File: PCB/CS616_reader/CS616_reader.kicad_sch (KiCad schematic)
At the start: 15 parts, among them J1 Conn_01x04_Socket, J2 Conn_01x04_Socket, J3 Conn_01x04_Socket, J4 Conn_01x04_Socket, J5 Conn_01x04_Socket, J6 Conn_01x04_Socket, J7 Conn_01x04_Socket, J8 Conn_01x04_Socket, J9 Conn_01x04_Socket, U1 CD4051B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

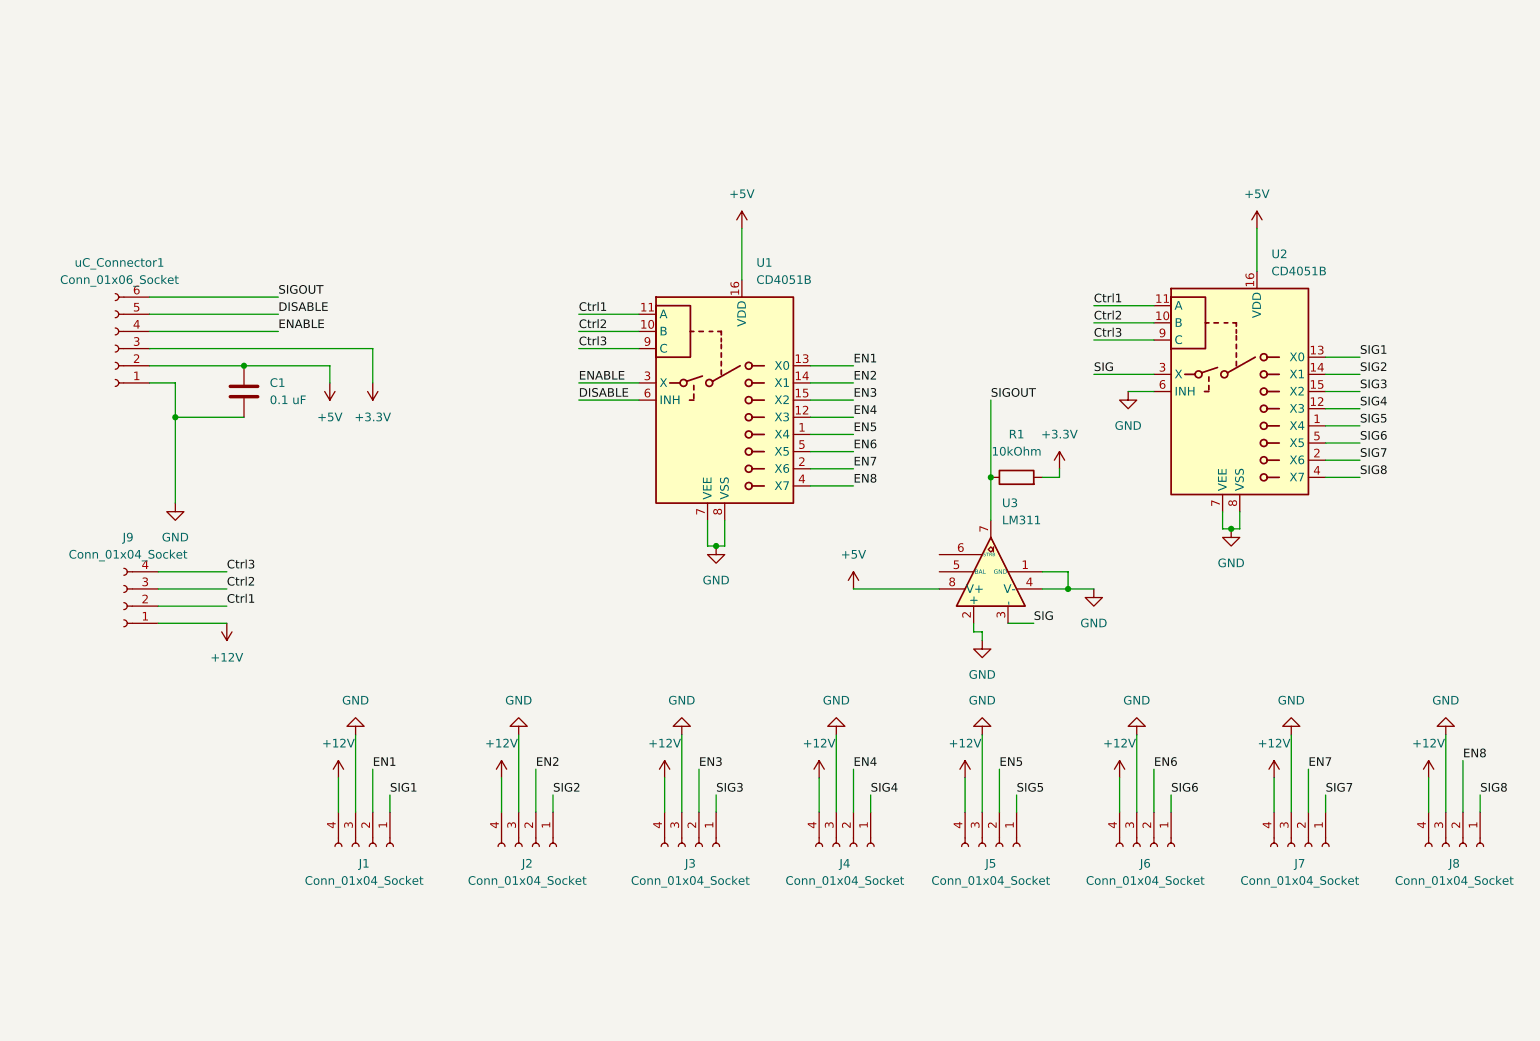
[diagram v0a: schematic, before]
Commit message: Added logic level converter to pcb
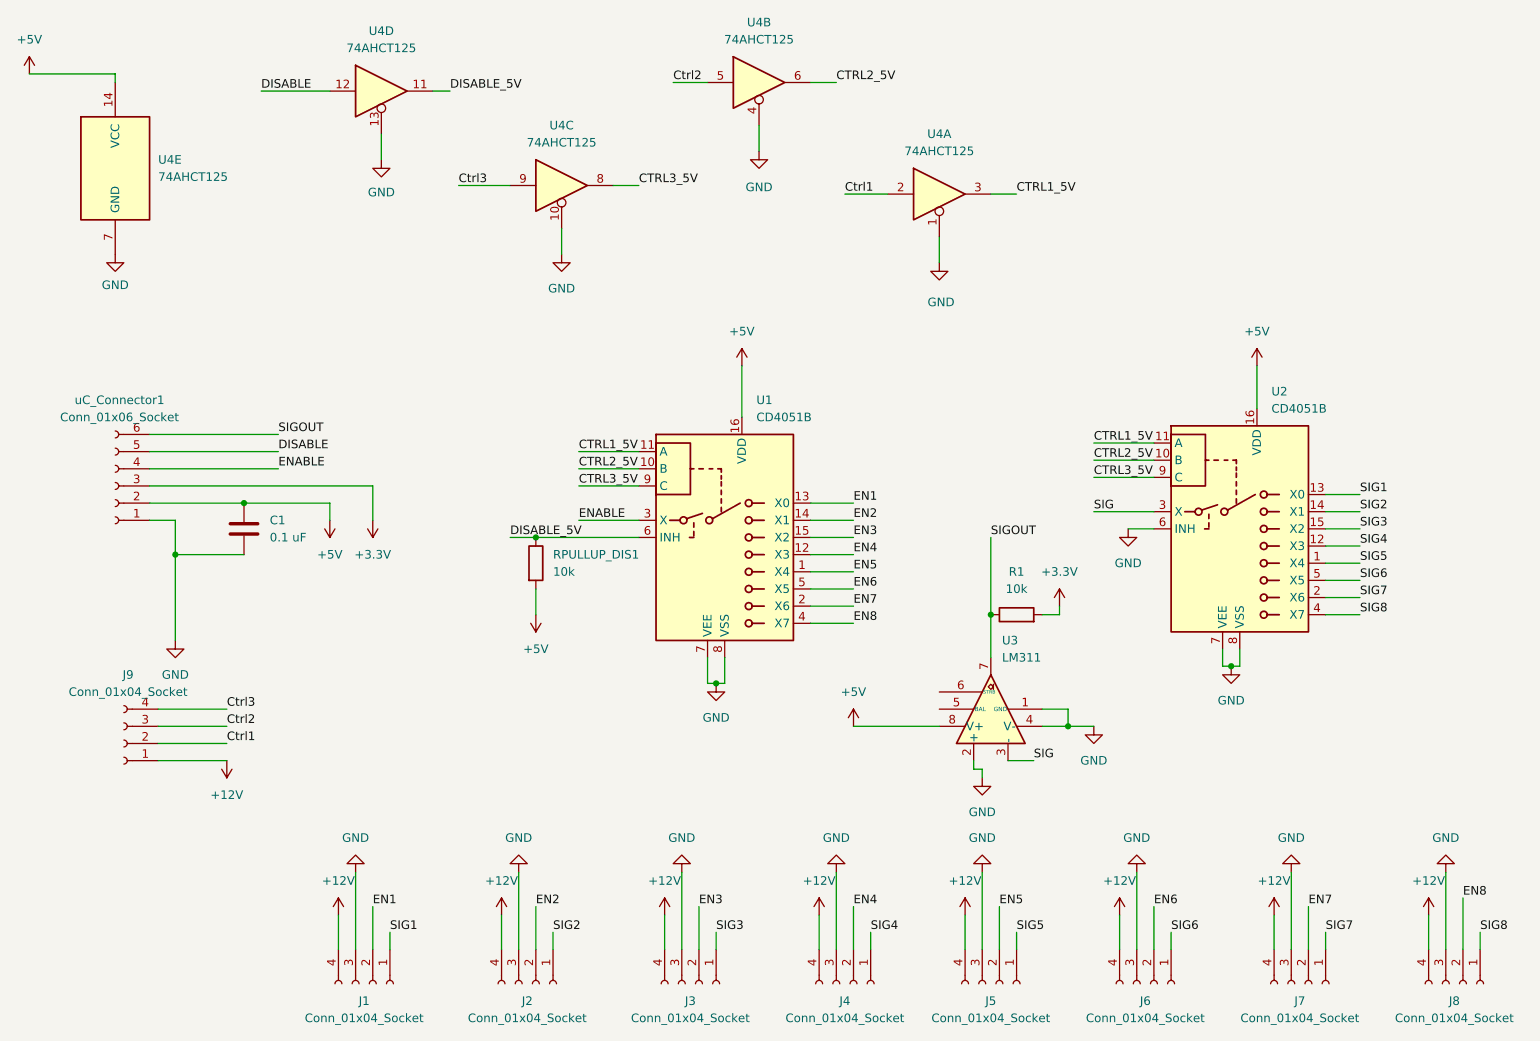
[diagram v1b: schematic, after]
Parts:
- added RPULLUP_DIS1: 10k, Resistor_THT:R_Axial_DIN0204_L3.6mm_D1.6mm_P5.08mm_Horizontal, symbol Device:R
- added U4: 74AHCT125, Package_DIP:DIP-14_W7.62mm, symbol 74xx:74AHCT125
- R1: value 10kOhm -> 10k
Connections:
- net +5V: now also RPULLUP_DIS1.2, U4.14 (VCC)
- net Ctrl1: now also U4.2; no longer U1.11 (A), U2.11 (A)
- net Ctrl2: now also U4.5; no longer U1.10 (B), U2.10 (B)
- net Ctrl3: now also U4.9; no longer U1.9 (C), U2.9 (C)
- net DISABLE: now also U4.12; no longer U1.6 (INH)
- net GND: now also U4.1, U4.10, U4.13, U4.4, U4.7 (GND)
- new net CTRL1_5V: U1.11 (A), U2.11 (A), U4.3
- new net CTRL2_5V: U1.10 (B), U2.10 (B), U4.6
- new net CTRL3_5V: U1.9 (C), U2.9 (C), U4.8
- new net DISABLE_5V: RPULLUP_DIS1.1, U1.6 (INH), U4.11
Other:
- moved on the sheet: C1, J1, J2, J3, J4, J5, J6, J7, J8, J9, R1, U1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
